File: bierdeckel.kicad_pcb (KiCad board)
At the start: 2 copper layers, 93 x 93 mm, 69 parts, among them IC1 HSFPAR004A, J1 Pogo, J2 Pogo, J6 USB-TYPE-C-020, SW1 PTS526 SK15 SMTR2 LFS, SW2 PTS526 SK15 SMTR2 LFS, SW3 PTS526 SK15 SMTR2 LFS, U1 ESP32-C3-WROOM-02, U2 BQ25176J, U3 TPS61201DRC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

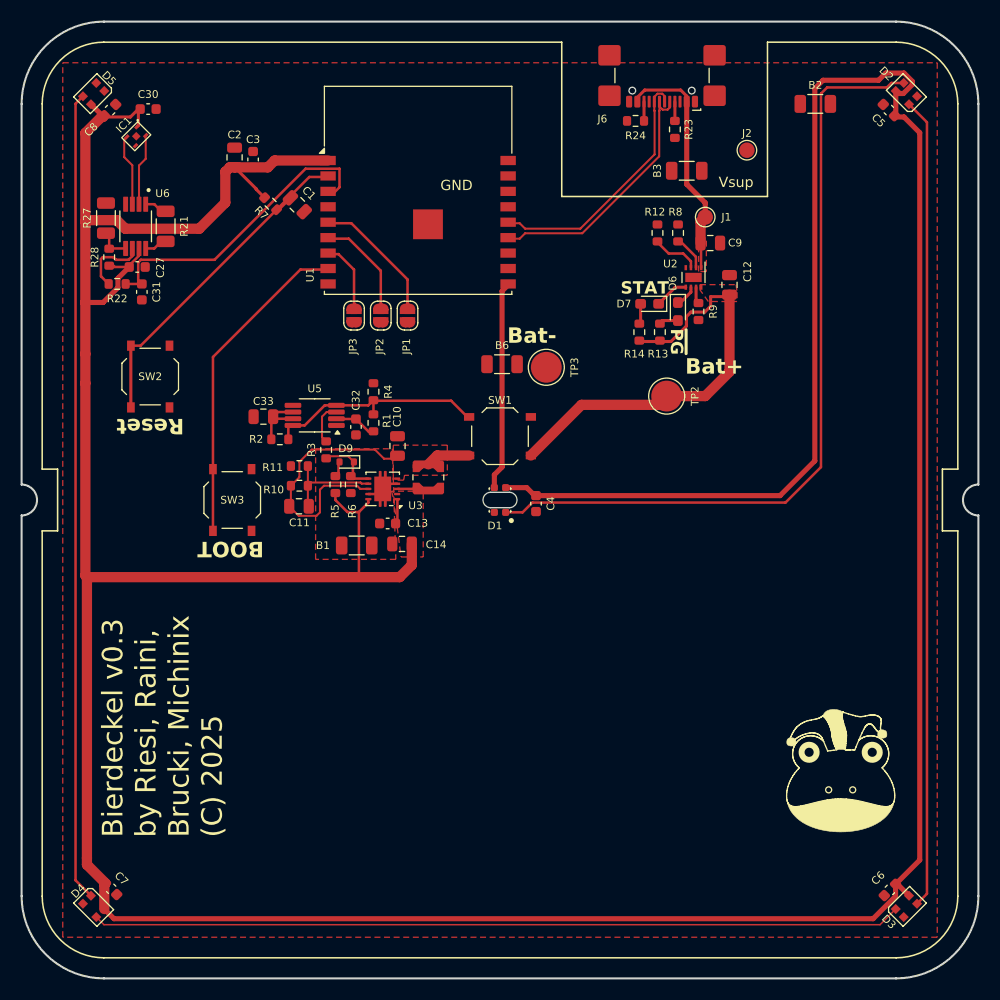
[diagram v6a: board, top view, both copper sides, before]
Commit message: change power ON and latching circuit to use FETs
should reduce leakage currents :)
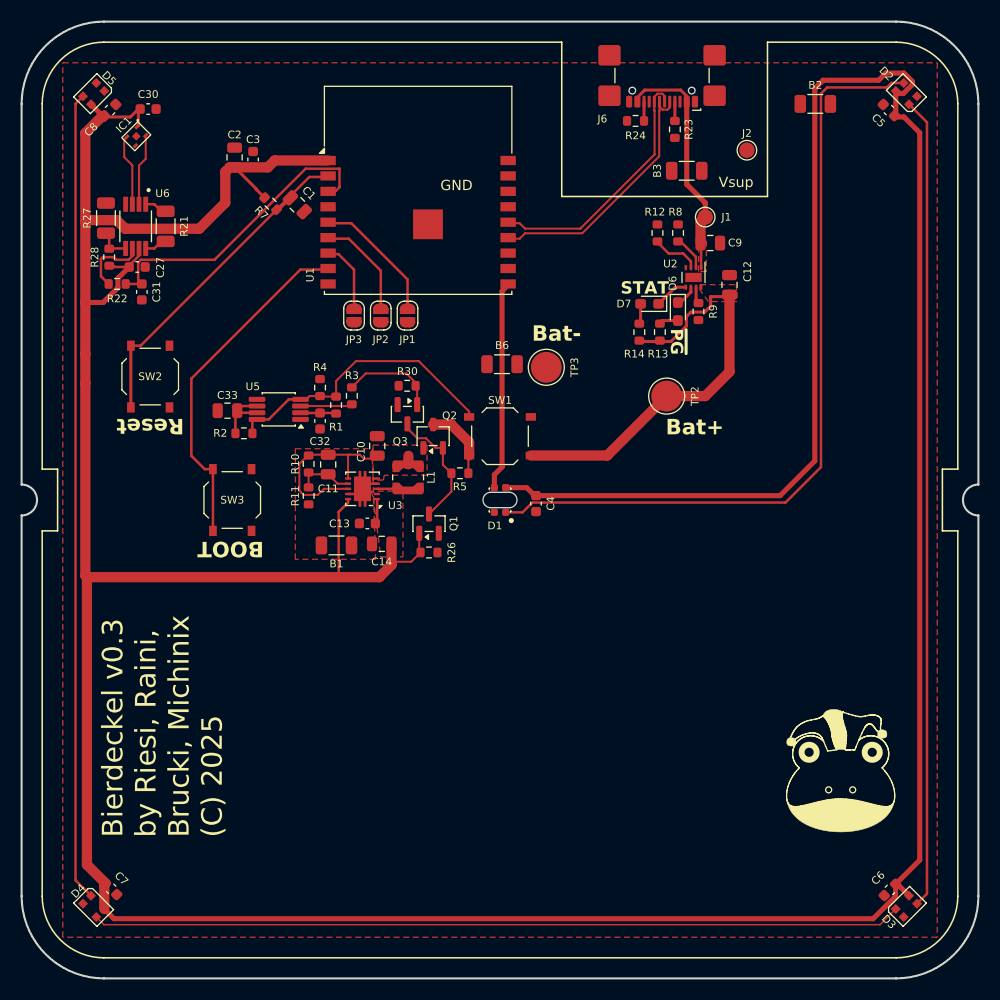
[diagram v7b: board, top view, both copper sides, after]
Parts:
- removed D9: 1N4148WT, Diode_SMD:D_SOD-523
- removed R6: 2.2M, Resistor_SMD:R_0603_1608Metric
- added Q1: BSS123, Package_TO_SOT_SMD:SOT-23, F.Cu at (139.6, 98.8)
- added Q2: SP20P18T1, Package_TO_SOT_SMD:SOT-23-3, F.Cu at (140.0, 90.3)
- added Q3: BSS123, Package_TO_SOT_SMD:SOT-23, F.Cu at (137.5, 88.2)
- added R26: 2.2M, Resistor_SMD:R_0603_1608Metric, F.Cu at (139.6, 101.6)
- added R30: 200k, Resistor_SMD:R_0603_1608Metric, F.Cu at (137.5, 85.4)
- R5: value 10k -> 200k
- moved R5 12.1 mm to (142.6, 93.9), turned to 180 degrees
- moved R3 5.81 mm to (132.1, 86.4), turned to -90 degrees
- moved R4 5.21 mm to (129.0, 85.6)
- moved C11 4.96 mm to (129.8, 93.0), turned to -90 degrees
- moved R1 4.02 mm to (130.6, 87.3)
- moved U5 3.54 mm to (125.0, 87.7)
- moved C32 3.54 mm to (129.0, 88.8)
- moved C33 3.54 mm to (120.0, 87.8)
- moved R2 3.54 mm to (121.6, 90.0)
- moved R11 3.04 mm to (127.9, 96.1), turned to -90 degrees
- moved R10 2.30 mm to (127.9, 93.0), turned to -90 degrees
- moved B1 1.97 mm to (130.6, 100.9)
- moved C10 1.97 mm to (134.6, 91.2)
- moved C13 1.97 mm to (133.6, 98.8)
- moved C14 1.97 mm to (135.0, 100.8)
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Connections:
- C12 pad 1: +BATT -> +BATT_EXT
- R13 pad 1: +BATT -> +BATT_EXT
- R14 pad 1: +BATT -> +BATT_EXT
- R3 pad 1: /PSU_EN -> /NE_TOGGLE_OUT
- R5 pad 1: Net-(D9-A) -> +BATT_EXT
- R5 pad 2: +3.3V -> Net-(Q1-D)
- SW1 pad 1: +BATT -> +BATT_EXT
- TP2 pad 1: +BATT -> +BATT_EXT
- U2 pad 8: +BATT -> +BATT_EXT
- U3 pad 6: /PSU_EN -> +BATT
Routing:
- net +BATT: track 72.1 -> 19.2 mm
- net +BATT_EXT: track 0.00 -> 49.1 mm
- net Net-(Q1-D): track 0.00 -> 12.3 mm
- net /NE_TOGGLE_OUT: track 0.00 -> 9.32 mm
- net /PSU_EN: track 6.31 -> 0.00 mm
- net Net-(U5-R): track 22.0 -> 28.2 mm
- net Net-(U3-UVLO): track 10.0 -> 5.73 mm
- net /~{BOOTLOADER}: track 31.6 -> 33.8 mm
- net Net-(D9-A): track 1.54 -> 0.00 mm
- net Net-(U5-Q): track 4.15 -> 5.02 mm
- net Net-(U5-TR): track 4.11 -> 3.49 mm
- added copper zone on F.Cu, net +BATT_EXT
